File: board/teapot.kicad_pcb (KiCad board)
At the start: 2 copper layers, 49.9 x 50 mm, 48 parts, among them J1 MICROUSB, P1 BATT, P2 SMA, P3 SWD_TC, Q1 TEPT4400, U1 TPS79333DBVR, U2 TLV61225, U4 RFM69W, U5 STM32L052K8, U6 HTU21D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

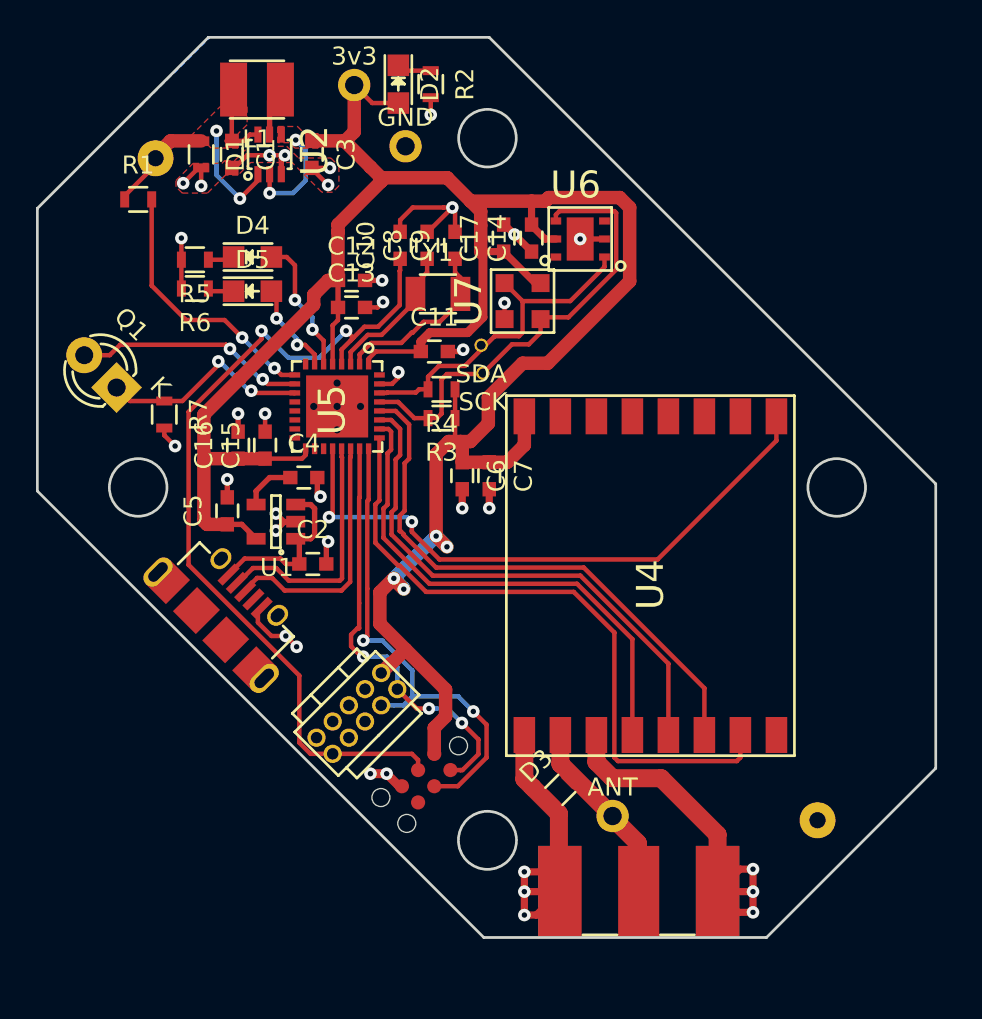
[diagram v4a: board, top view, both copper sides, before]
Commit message: Moved mounting holes. Fixes #10
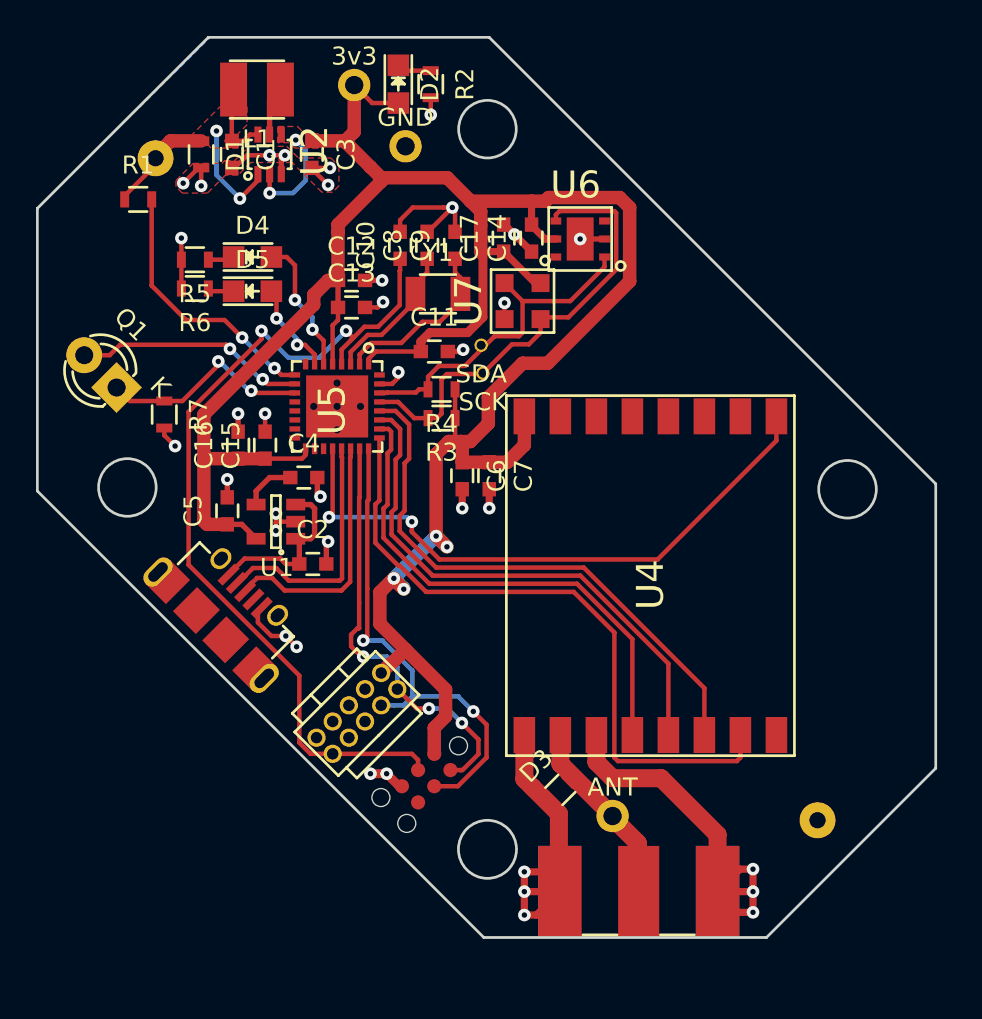
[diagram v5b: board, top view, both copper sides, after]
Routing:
- net GND: track 89.3 -> 88.8 mm
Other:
- outline, holes or cut-outs redrawn
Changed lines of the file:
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@@
-(kicad_pcb (version 4) (host pcbnew 4.0.1-3.201512150931+6195~38~ubuntu14.04.1-stable)
+(kicad_pcb (version 4) (host pcbnew 0.201509071501+6164~29~ubuntu14.04.1-product)
   (general
     (links 125)
@@
     (area 100.070058 86.662048 153.387952 140.489)
     (thickness 1.6)
-    (drawings 16)
-    (tracks 568)
+    (drawings 18)
+    (tracks 563)
     (zones 0)
     (modules 48)
@@
     (pad_to_mask_clearance 0.2)
     (aux_axis_origin 0 0)
-    (visible_elements FFFFFF5F)
+    (visible_elements FFFFFFFF)
     (pcbplotparams
       (layerselection 0x010f0_80000001)
@@
     (pad "" thru_hole oval (at -4.175 0 315) (size 1 1.9) (drill oval 0.6 1.3) (layers *.Cu *.Mask F.SilkS))
   )
+  (gr_circle (center 107 113) (end 107.1 113) (layer F.Fab) (width 0.2))
+  (gr_circle (center 147 113.1) (end 147.1 113.1) (layer F.Fab) (width 0.2))
   (gr_line (start 126.8 138) (end 142.5 138) (angle 90) (layer Edge.Cuts) (width 0.15))
   (gr_line (start 142.5 138) (end 151.9 128.6) (angle 90) (layer Edge.Cuts) (width 0.15))
@@
   (gr_line (start 102 113.2) (end 126.8 138) (angle 90) (layer Edge.Cuts) (width 0.15))
   (gr_line (start 127.1 88) (end 151.9 112.8) (angle 90) (layer Edge.Cuts) (width 0.15))
-  (gr_circle (center 146.4 113) (end 148.8 113) (layer F.CrtYd) (width 0.2))
-  (gr_circle (center 127 93.6) (end 129.4 93.6) (layer F.CrtYd) (width 0.2))
-  (gr_circle (center 107.6 113) (end 110 113) (layer F.CrtYd) (width 0.2))
-  (gr_circle (center 127 132.6) (end 129.4 132.6) (layer F.CrtYd) (width 0.2))
-  (gr_circle (center 127 132.6) (end 128.6 132.4) (layer Edge.Cuts) (width 0.15))
-  (gr_circle (center 146.4 113) (end 148 113) (layer Edge.Cuts) (width 0.15))
-  (gr_circle (center 127 93.6) (end 128.6 93.6) (layer Edge.Cuts) (width 0.15))
-  (gr_circle (center 107.6 113) (end 109.2 113) (layer Edge.Cuts) (width 0.15))
+  (gr_circle (center 147 113.1) (end 149.4 113.1) (layer F.CrtYd) (width 0.2))
+  (gr_circle (center 127 93.1) (end 129.4 93.1) (layer F.CrtYd) (width 0.2))
+  (gr_circle (center 107 113) (end 109.4 113) (layer F.CrtYd) (width 0.2))
+  (gr_circle (center 127 133.1) (end 129.4 133.1) (layer F.CrtYd) (width 0.2))
+  (gr_circle (center 127 133.1) (end 128.6 132.9) (layer Edge.Cuts) (width 0.15))
+  (gr_circle (center 147 113.1) (end 148.6 113.1) (layer Edge.Cuts) (width 0.15))
+  (gr_circle (center 127 93.1) (end 128.6 93.1) (layer Edge.Cuts) (width 0.15))
+  (gr_circle (center 107 113) (end 108.6 113) (layer Edge.Cuts) (width 0.15))
   (gr_line (start 111.5 88) (end 102 97.5) (angle 90) (layer Edge.Cuts) (width 0.15))
   (segment (start 116.9 111.2) (end 116.7 111.4) (width 0.25) (layer F.Cu) (net 1))
@@
   (segment (start 114.25 95.55) (end 114.25 95.6) (width 0.25) (layer F.Cu) (net 2))
   (segment (start 112.8 93.8) (end 112.8 93.75) (width 0.25) (layer F.Cu) (net 2))
+  (segment (start 115.25 114.45) (end 115.25 114.948272) (width 0.25) (layer F.Cu) (net 3))
+  (segment (start 115.25 114.948272) (end 115.25 115.4) (width 0.25) (layer F.Cu) (net 3))
+  (segment (start 116.35 114.9) (end 115.298272 114.9) (width 0.25) (layer F.Cu) (net 3))
+  (segment (start 115.298272 114.9) (end 115.25 114.948272) (width 0.25) (layer F.Cu) (net 3))
   (segment (start 121.7 107.25) (end 122.05 106.9) (width 0.25) (layer F.Cu) (net 3))
   (via (at 122.05 106.6) (size 0.7) (drill 0.3) (layers F.Cu B.Cu) (net 3))
@@
   (segment (start 112.55 113.55) (end 112.55 112.55) (width 0.3) (layer F.Cu) (net 3))
   (via (at 112.55 112.55) (size 0.7) (drill 0.3) (layers F.Cu B.Cu) (net 3))
-  (segment (start 116.35 114.9) (end 115.75 114.9) (width 0.3) (layer F.Cu) (net 3))
-  (segment (start 115.75 114.9) (end 115.25 115.4) (width 0.3) (layer F.Cu) (net 3))
   (via (at 115.25 115.4) (size 0.7) (drill 0.3) (layers F.Cu B.Cu) (net 3))
-  (segment (start 116.35 114.9) (end 115.7 114.9) (width 0.3) (layer F.Cu) (net 3))
-  (segment (start 115.7 114.9) (end 115.25 114.45) (width 0.3) (layer F.Cu) (net 3))
   (via (at 115.25 114.45) (size 0.7) (drill 0.3) (layers F.Cu B.Cu) (net 3))
   (segment (start 118.05 117.25) (end 118.05 116.1) (width 0.3) (layer F.Cu) (net 3))
@@
   (segment (start 123.65 101.05) (end 123.65 100.3) (width 0.25) (layer F.Cu) (net 11))
   (segment (start 123 102.25) (end 123 101.7) (width 0.25) (layer F.Cu) (net 11))
-  (segment (start 123.450046 103.799989) (end 124.350011 103.799989) (width 0.25) (layer F.Cu) (net 12))
+  (segment (start 119.9 106.15) (end 119.9 105.614998) (width 0.25) (layer F.Cu) (net 12))
+  (segment (start 122.215008 104.97499) (end 123.390009 103.799989) (width 0.25) (layer F.Cu) (net 12))
+  (segment (start 119.9 105.614998) (end 120.540008 104.97499) (width 0.25) (layer F.Cu) (net 12))
+  (segment (start 120.540008 104.97499) (end 122.215008 104.97499) (width 0.25) (layer F.Cu) (net 12))
+  (segment (start 123.390009 103.799989) (end 124.350011 103.799989) (width 0.25) (layer F.Cu) (net 12))
   (segment (start 124.350011 103.799989) (end 125.5 102.65) (width 0.25) (layer F.Cu) (net 12))
   (segment (start 125.5 102.65) (end 125.5 102.25) (width 0.25) (layer F.Cu) (net 12))
-  (segment (start 120.540008 104.97499) (end 122.215008 104.97499) (width 0.25) (layer F.Cu) (net 12))
-  (segment (start 122.215008 104.97499) (end 122.789998 104.4) (width 0.25) (layer F.Cu) (net 12))
-  (segment (start 122.789998 104.4) (end 122.850035 104.4) (width 0.25) (layer F.Cu) (net 12))
-  (segment (start 122.850035 104.4) (end 123.450046 103.799989) (width 0.25) (layer F.Cu) (net 12))
-  (segment (start 119.9 106.15) (end 119.9 105.614998) (width 0.25) (layer F.Cu) (net 12))
-  (segment (start 119.9 105.614998) (end 120.540008 104.97499) (width 0.25) (layer F.Cu) (net 12))
   (segment (start 125.5 101.35) (end 125.2 101.05) (width 0.25) (layer F.Cu) (net 12))
   (segment (start 125.2 101.05) (end 125.2 100.3) (width 0.25) (layer F.Cu) (net 12))
@@
   (segment (start 132.16361 117.90002) (end 137.05 122.78641) (width 0.25) (layer F.Cu) (net 19))
   (segment (start 137.05 122.78641) (end 137.05 126.75) (width 0.25) (layer F.Cu) (net 19))
-  (segment (start 132.35001 117.45001) (end 139.05 124.15) (width 0.25) (layer F.Cu) (net 20))
-  (segment (start 139.05 124.15) (end 139.05 126.75) (width 0.25) (layer F.Cu) (net 20))
-  (segment (start 122.125005 115.4272) (end 122.1772 115.4272) (width 0.25) (layer F.Cu) (net 20))
-  (segment (start 122.1772 115.4272) (end 122.350005 115.600005) (width 0.25) (layer F.Cu) (net 20))
-  (segment (start 122.350005 115.600005) (end 122.350006 115.652201) (width 0.25) (layer F.Cu) (net 20))
-  (segment (start 122.350006 115.652201) (end 124.147815 117.45001) (width 0.25) (layer F.Cu) (net 20))
-  (segment (start 124.147815 117.45001) (end 132.35001 117.45001) (width 0.25) (layer F.Cu) (net 20))
   (segment (start 121 108.75) (end 121.9 108.75) (width 0.25) (layer F.Cu) (net 20))
+  (segment (start 122.125005 114.574995) (end 122.125005 115.4272) (width 0.25) (layer F.Cu) (net 20))
   (segment (start 121.9 108.75) (end 122.65 109.5) (width 0.25) (layer F.Cu) (net 20))
   (segment (start 122.65 109.5) (end 122.65 111.4) (width 0.25) (layer F.Cu) (net 20))
   (segment (start 122.65 111.4) (end 122.4 111.65) (width 0.25) (layer F.Cu) (net 20))
   (segment (start 122.4 111.65) (end 122.4 114.3) (width 0.25) (layer F.Cu) (net 20))
-  (segment (start 122.125005 114.574995) (end 122.125005 115.4272) (width 0.25) (layer F.Cu) (net 20))
   (segment (start 122.4 114.3) (end 122.125005 114.574995) (width 0.25) (layer F.Cu) (net 20))
+  (segment (start 122.125005 115.4272) (end 124.147815 117.45001) (width 0.25) (layer F.Cu) (net 20))
+  (segment (start 124.147815 117.45001) (end 132.35001 117.45001) (width 0.25) (layer F.Cu) (net 20))
+  (segment (start 132.35001 117.45001) (end 139.05 124.15) (width 0.25) (layer F.Cu) (net 20))
+  (segment (start 139.05 124.15) (end 139.05 126.75) (width 0.25) (layer F.Cu) (net 20))
   (segment (start 121 110.25) (end 121 113.721065) (width 0.25) (layer F.Cu) (net 21))
   (segment (start 121 113.721065) (end 120.774975 113.94609) (width 0.25) (layer F.Cu) (net 21))

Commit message: Moved antenna a bit, worked on silk
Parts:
- P3: value SWD_TC -> Tag-Connect
- moved TP1 1.75 mm to (132.2, 131.2)
- moved D3 1.10 mm to (130.1, 129.3), turned to 0 degrees
- moved TP3 0.55 mm to (123.0, 94.0)
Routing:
- net Net-(D3-Pad2): track 11.8 -> 15.5 mm
- net GND: track 88.8 -> 87.6 mm
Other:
- rule trace_min: 0.2 -> 0.15
- board text added: "0.8-3.3V DC"
- board text added: "2016-01-05"
- board text added: "ERR"
- board text added: "LIGHT"
- board text added: "PRESSURE"
- board text added: "RX"
- board text added: "TEAPOT r1"
- board text added: "TEMP+HUM"
- board text added: "david.w.turner@cl.cam.ac.uk dwt27.co.uk/teapot ukhas.net"
- board text added: "dwt27"

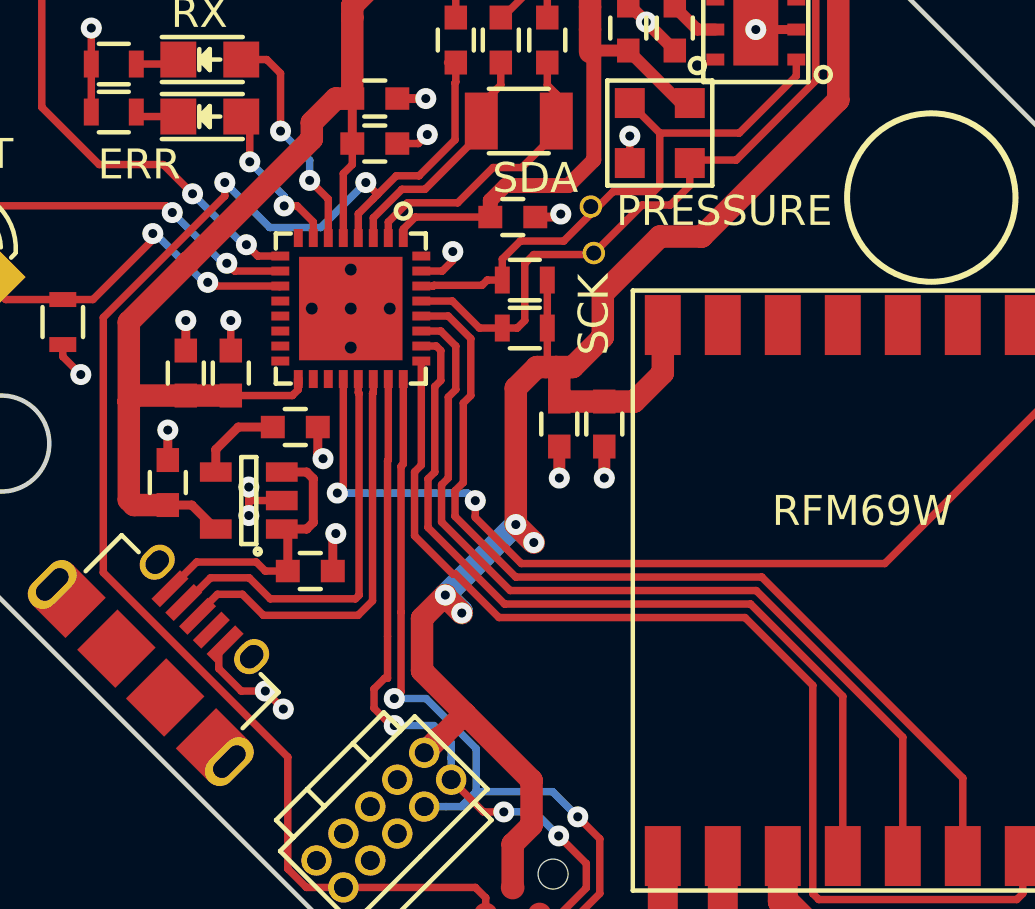
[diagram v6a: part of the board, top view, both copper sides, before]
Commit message: Fixed DRC clearance bugs
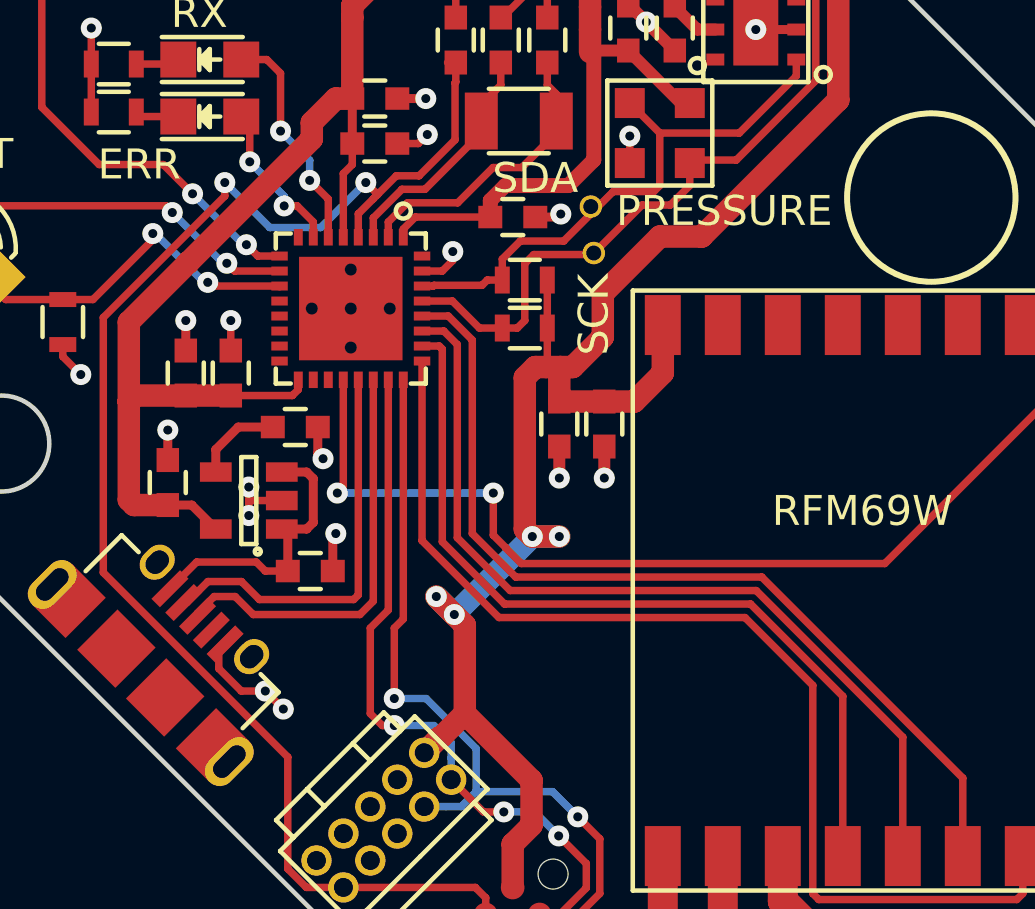
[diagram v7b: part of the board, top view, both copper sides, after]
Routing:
- net +3V3: track 145.9 -> 145.2 mm
- net /RFM_RESET: track 34.1 -> 34.6 mm
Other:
- rule trace_min: 0.15 -> 0.2032

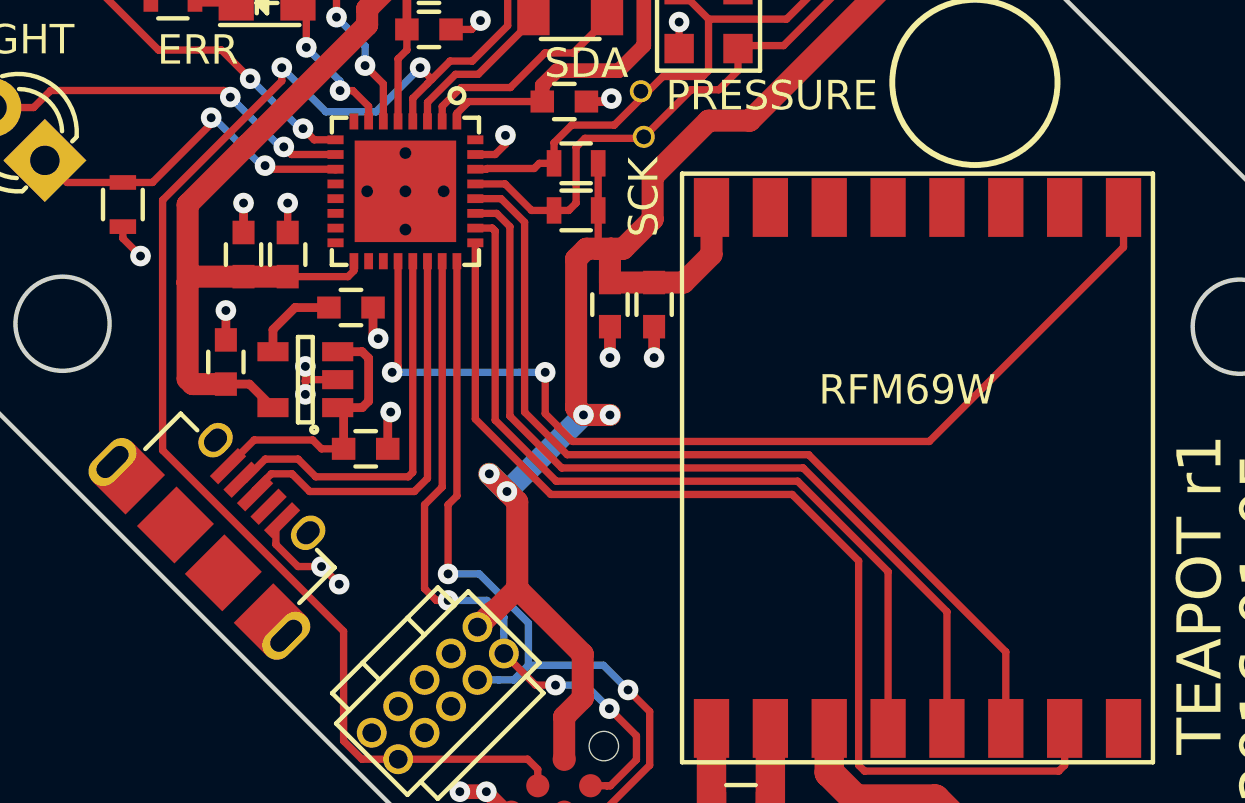
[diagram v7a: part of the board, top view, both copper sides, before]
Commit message: Added DIO0,4. Fixes #12
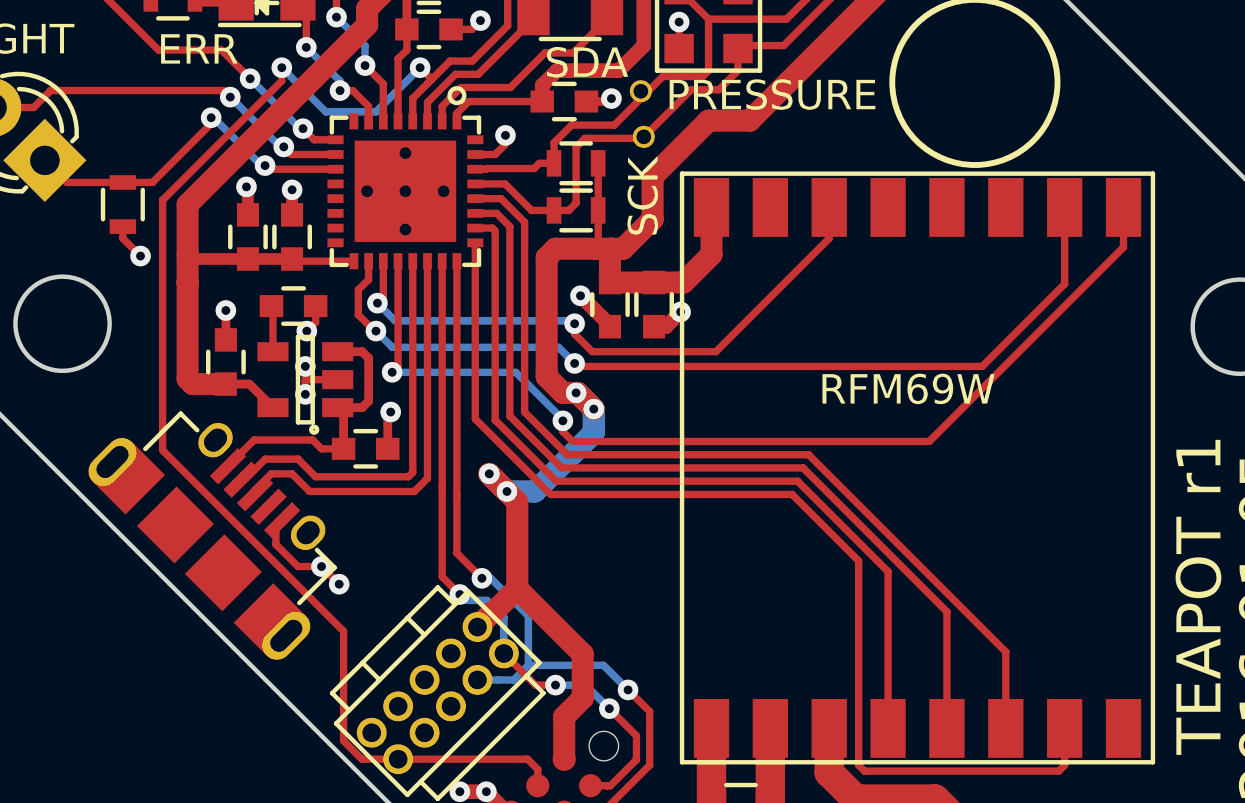
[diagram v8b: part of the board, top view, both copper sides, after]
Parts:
- P3: value Tag-Connect -> SWD_TC
- moved C4 1.95 mm to (114.8, 112.4)
- moved C15 0.62 mm to (114.8, 110.0)
- moved C16 0.62 mm to (113.3, 110.0)
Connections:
- U4 pad 2: (no net) -> /RFM_DIO0
- U4 pad 6: (no net) -> /RFM_DIO4
- U5 pad 18: (no net) -> /RFM_DIO0
- U5 pad 19: (no net) -> /RFM_DIO4
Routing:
- net /RFM_DIO0: track 0.00 -> 30.5 mm, vias 0 -> 2
- net /RFM_DIO4: track 0.00 -> 21.9 mm, vias 0 -> 2
- net Net-(C4-Pad1): track 2.96 -> 1.57 mm
- net +3V3: track 145.2 -> 146.4 mm
- net /SWDIO: track 24.4 -> 23.2 mm
- net /SWCLK: track 27.7 -> 27.0 mm
- net /RFM_RESET: track 34.6 -> 34.0 mm
